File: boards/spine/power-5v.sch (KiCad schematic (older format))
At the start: 15 parts, among them U8 RT8299A

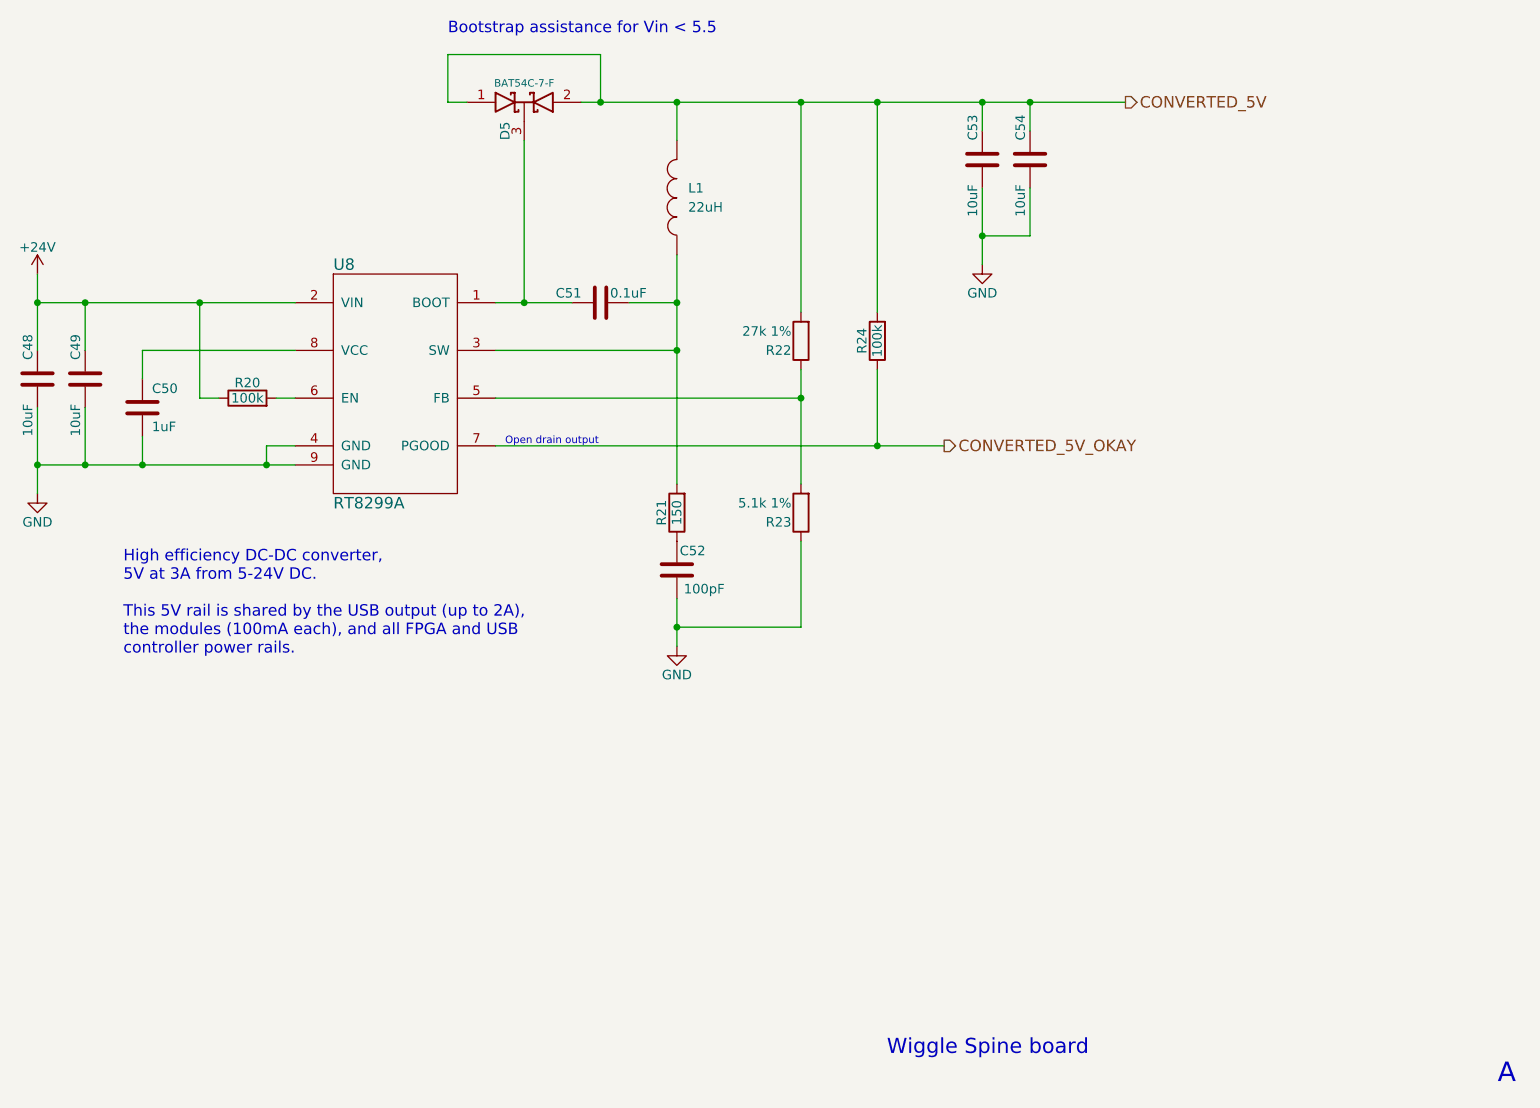
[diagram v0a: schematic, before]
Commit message: Capacitor upgrades, BOM tidying
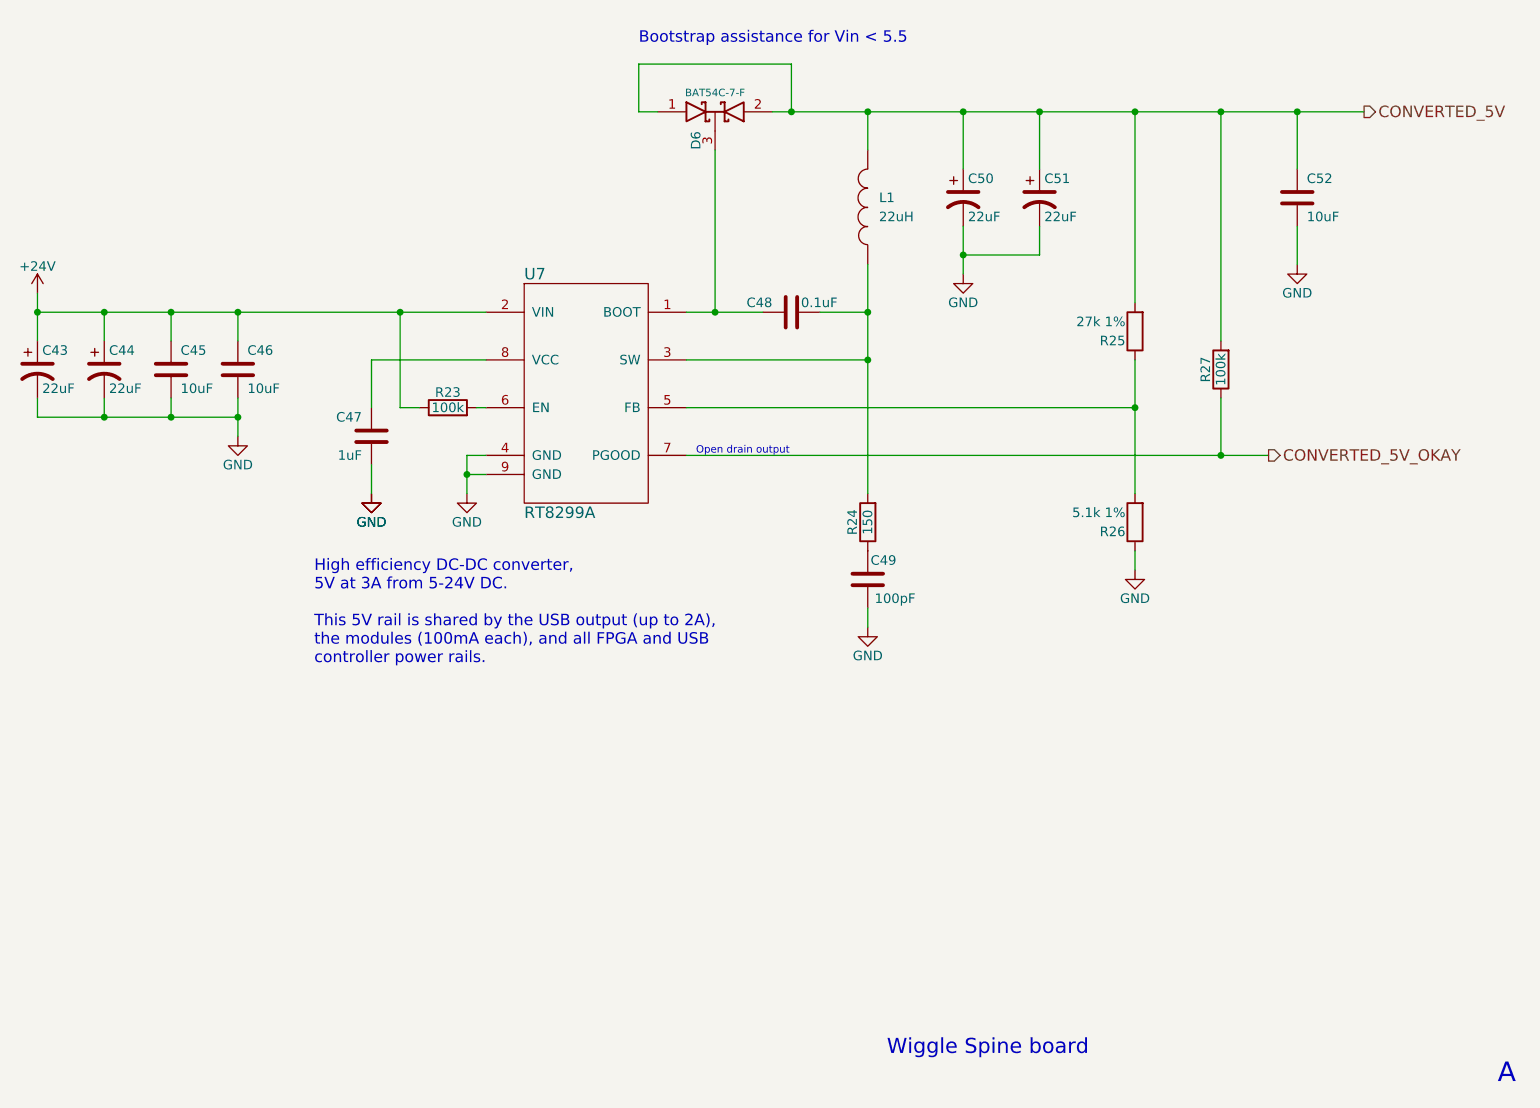
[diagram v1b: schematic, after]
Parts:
- removed C48, C49, C53, C54: 10uF, Capacitors_SMD:C_1206, symbol C
- added C43, C44, C50, C51: 22uF, Capacitors_SMD:c_elec_6.3x7.7, symbol CP1
- added C45, C46, C52: 10uF, Capacitors_SMD:C_1206, symbol C
- C47: renamed from C50; value 1uF -> 1uF
- renumbered C51 to C48, C52 to C49, D5 to D6, R20 to R23, R21 to R24, R22 to R25, R23 to R26, R24 to R27, U8 to U7
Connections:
- net +24V: now also C43.1, C44.1, C45.1, C46.1
- net CONVERTED_5V: now also C50.1, C51.1, C52.1
- net GND: now also C43.2, C44.2, C45.2, C46.2, C50.2, C51.2, C52.2
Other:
- moved on the sheet: C47, C48, C49, D6, L1, R23, R24, R25, R26, R27, U7

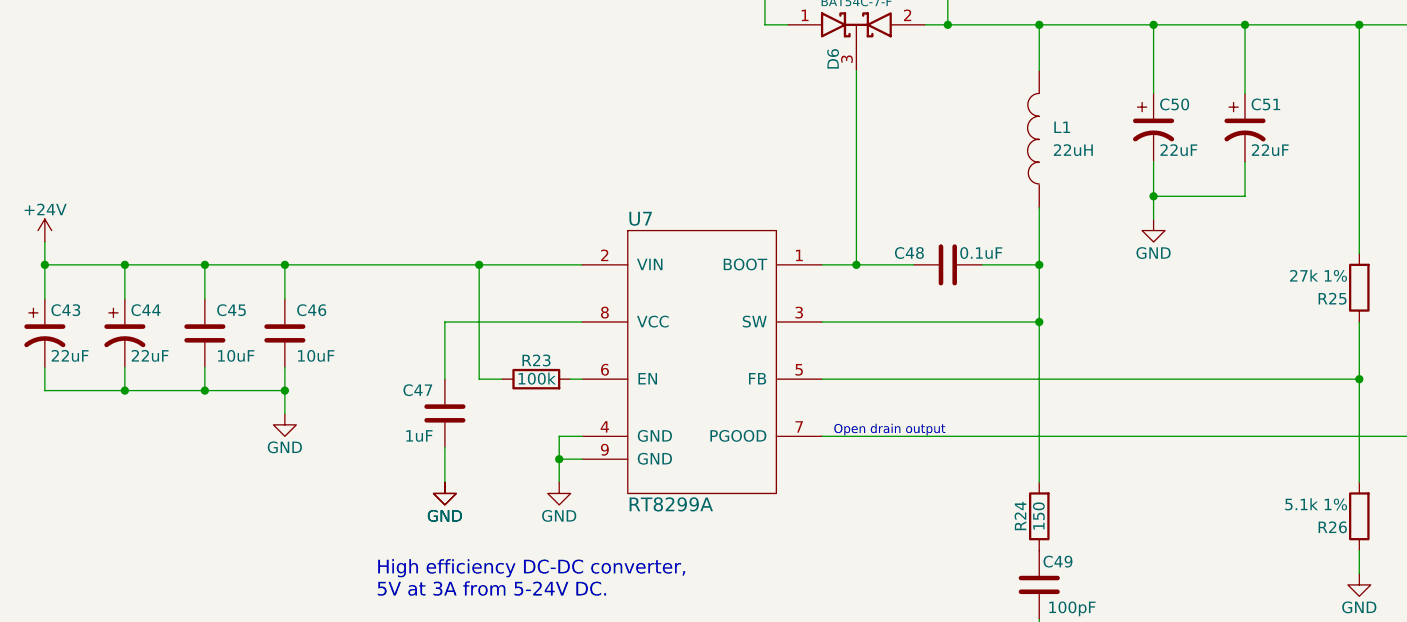
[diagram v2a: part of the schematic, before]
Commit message: Schematics stabilizing for next proto, starting PCB updates
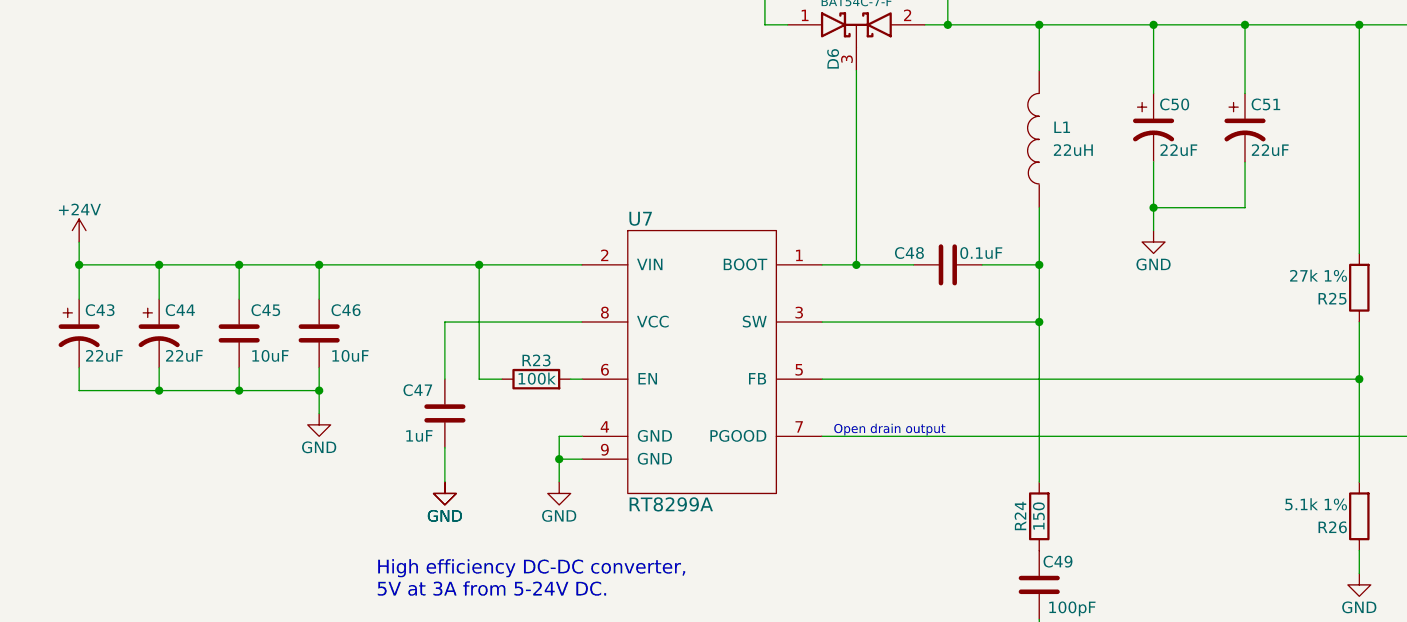
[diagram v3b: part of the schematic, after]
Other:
- moved on the sheet: C43, C44, C45, C46
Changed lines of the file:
@@
 L +24V #PWR0123
 U 1 1 564CA8DB
-P 2250 3750
-F 0 "#PWR0123" H 2250 3600 50  0001 C CNN
-F 1 "+24V" H 2250 3890 50  0000 C CNN
-F 2 "" H 2250 3750 60  0000 C CNN
-F 3 "" H 2250 3750 60  0000 C CNN
-	1    2250 3750
+P 2400 3750
+F 0 "#PWR0123" H 2400 3600 50  0001 C CNN
+F 1 "+24V" H 2400 3890 50  0000 C CNN
+F 2 "" H 2400 3750 60  0000 C CNN
+F 3 "" H 2400 3750 60  0000 C CNN
+	1    2400 3750
 	1    0    0    -1
 $EndComp
@@
 FB 59 00 E6 A5 69 3A 37 9E CF 73 BC F7 37 E3 33 5D 9E A8 3E 7F 80 FA F7 F6 BB 44 F4 6E D4 E7 77
 A2 1E 1F 27 A2 E3 16 70 32 E9 54 FE 3F E7 AF 00 CA 1C A3 36 0A 00 00 00 00 49 45 4E 44 AE 42 60
-82 00
+82 70
 EndData
 $EndBitmap
@@
 L GND #PWR0126
 U 1 1 567A1422
-P 7100 3650
-F 0 "#PWR0126" H 7100 3400 50  0001 C CNN
-F 1 "GND" H 7100 3500 50  0000 C CNN
-F 2 "" H 7100 3650 60  0000 C CNN
-F 3 "" H 7100 3650 60  0000 C CNN
-	1    7100 3650
+P 7100 3700
+F 0 "#PWR0126" H 7100 3450 50  0001 C CNN
+F 1 "GND" H 7100 3550 50  0000 C CNN
+F 2 "" H 7100 3700 60  0000 C CNN
+F 3 "" H 7100 3700 60  0000 C CNN
+	1    7100 3700
 	1    0    0    -1
 $EndComp
@@
 Wire Wire Line
 	4000 4100 4600 4100
-Connection ~ 3300 3850
-Wire Wire Line
-	3300 3850 3300 4000
-Wire Wire Line
-	2250 3850 4600 3850
+Connection ~ 3450 3850
+Wire Wire Line
+	3450 3850 3450 4000
 Wire Wire Line
 	5650 3850 6050 3850
 Wire Wire Line
-	4150 4350 4150 3850
+	4150 3850 4150 4350
 Connection ~ 4150 3850
 Wire Wire Line
-	7100 3400 7100 3650
-Wire Wire Line
-	7100 3550 7500 3550
-Wire Wire Line
-	7500 3550 7500 3400
-Connection ~ 7100 3550
+	7100 3400 7100 3700
+Wire Wire Line
+	7100 3600 7500 3600
+Wire Wire Line
+	7500 3600 7500 3400
+Connection ~ 7100 3600
 Wire Wire Line
 	7100 3100 7100 2800
@@
 	4550 4350 4600 4350
 Wire Wire Line
-	4250 4350 4150 4350
+	4150 4350 4250 4350
 $Comp
 L CP1 C43
 U 1 1 567A2C4C
-P 2250 4150
-F 0 "C43" H 2275 4250 50  0000 L CNN
-F 1 "22uF" H 2275 4050 50  0000 L CNN
-F 2 "Capacitors_SMD:c_elec_6.3x7.7" H 2250 4150 60  0001 C CNN
-F 3 "http://nichicon-us.com/english/products/pdfs/e-cd.pdf" H 2250 4150 60  0001 C CNN
-F 4 "Digikey" H 2250 4150 60  0001 C CNN "Vend1"
-F 5 "493-6180-2-ND" H 2250 4150 60  0001 C CNN "Vend1Id"
-F 6 "Nichicon" H 2250 4150 60  0001 C CNN "Mfg1"
-F 7 "UCD1H220MCL1GS" H 2250 4150 60  0001 C CNN "Mfg1Id"
-F 8 "0.10868" H 2250 4150 60  0001 C CNN "RefPrice1k"
-	1    2250 4150
+P 2400 4150
+F 0 "C43" H 2425 4250 50  0000 L CNN
+F 1 "22uF" H 2425 4050 50  0000 L CNN
+F 2 "Capacitors_SMD:c_elec_6.3x7.7" H 2400 4150 60  0001 C CNN
+F 3 "http://nichicon-us.com/english/products/pdfs/e-cd.pdf" H 2400 4150 60  0001 C CNN
+F 4 "Digikey" H 2400 4150 60  0001 C CNN "Vend1"
+F 5 "493-6180-2-ND" H 2400 4150 60  0001 C CNN "Vend1Id"
+F 6 "Nichicon" H 2400 4150 60  0001 C CNN "Mfg1"
+F 7 "UCD1H220MCL1GS" H 2400 4150 60  0001 C CNN "Mfg1Id"
+F 8 "0.10868" H 2400 4150 60  0001 C CNN "RefPrice1k"
+	1    2400 4150
 	1    0    0    -1
 $EndComp
@@
 L CP1 C44
 U 1 1 567A2CD8
-P 2600 4150
-F 0 "C44" H 2625 4250 50  0000 L CNN
-F 1 "22uF" H 2625 4050 50  0000 L CNN
-F 2 "Capacitors_SMD:c_elec_6.3x7.7" H 2600 4150 60  0001 C CNN
-F 3 "http://nichicon-us.com/english/products/pdfs/e-cd.pdf" H 2600 4150 60  0001 C CNN
-F 4 "Digikey" H 2600 4150 60  0001 C CNN "Vend1"
-F 5 "493-6180-2-ND" H 2600 4150 60  0001 C CNN "Vend1Id"
-F 6 "Nichicon" H 2600 4150 60  0001 C CNN "Mfg1"
-F 7 "UCD1H220MCL1GS" H 2600 4150 60  0001 C CNN "Mfg1Id"
-F 8 "0.10868" H 2600 4150 60  0001 C CNN "RefPrice1k"
-	1    2600 4150
+P 2750 4150
+F 0 "C44" H 2775 4250 50  0000 L CNN
+F 1 "22uF" H 2775 4050 50  0000 L CNN
+F 2 "Capacitors_SMD:c_elec_6.3x7.7" H 2750 4150 60  0001 C CNN
+F 3 "http://nichicon-us.com/english/products/pdfs/e-cd.pdf" H 2750 4150 60  0001 C CNN
+F 4 "Digikey" H 2750 4150 60  0001 C CNN "Vend1"
+F 5 "493-6180-2-ND" H 2750 4150 60  0001 C CNN "Vend1Id"
+F 6 "Nichicon" H 2750 4150 60  0001 C CNN "Mfg1"
+F 7 "UCD1H220MCL1GS" H 2750 4150 60  0001 C CNN "Mfg1Id"
+F 8 "0.10868" H 2750 4150 60  0001 C CNN "RefPrice1k"
+	1    2750 4150
 	1    0    0    -1
 $EndComp
@@
 L C C46
 U 1 1 567A30F9
-P 3300 4150
-F 0 "C46" H 3350 4250 50  0000 L CNN
-F 1 "10uF " H 3350 4050 50  0000 L CNN
-F 2 "Capacitors_SMD:C_1206" H 3338 4000 30  0001 C CNN
-F 3 "http://www.murata.com/~/media/webrenewal/support/library/catalog/products/capacitor/mlcc/c02e.ashx" H 3300 4150 60  0001 C CNN
-F 4 "GRM31CR61H106MA12L" H 3350 3950 39  0001 L BNN "Mfg1Id"
-F 5 "Murata" H 3300 4150 60  0001 C CNN "Mfg1"
-F 6 "Digikey" H 3300 4150 60  0001 C CNN "Vend1"
-F 7 "490-10756-2-ND" H 3300 4150 60  0001 C CNN "Vend1Id"
-F 8 "0.07429" H 3300 4150 60  0001 C CNN "RefPrice1k"
-	1    3300 4150
+P 3450 4150
+F 0 "C46" H 3500 4250 50  0000 L CNN
+F 1 "10uF " H 3500 4050 50  0000 L CNN
+F 2 "Capacitors_SMD:C_1206" H 3488 4000 30  0001 C CNN
+F 3 "http://www.murata.com/~/media/webrenewal/support/library/catalog/products/capacitor/mlcc/c02e.ashx" H 3450 4150 60  0001 C CNN
+F 4 "GRM31CR61H106MA12L" H 3500 3950 39  0001 L BNN "Mfg1Id"
+F 5 "Murata" H 3450 4150 60  0001 C CNN "Mfg1"
+F 6 "Digikey" H 3450 4150 60  0001 C CNN "Vend1"
+F 7 "490-10756-2-ND" H 3450 4150 60  0001 C CNN "Vend1Id"
+F 8 "0.07429" H 3450 4150 60  0001 C CNN "RefPrice1k"
+	1    3450 4150
 	1    0    0    -1
 $EndComp
@@
 L GND #PWR0131
 U 1 1 567A3822
-P 3300 4500
-F 0 "#PWR0131" H 3300 4250 50  0001 C CNN
-F 1 "GND" H 3300 4350 50  0000 C CNN
-F 2 "" H 3300 4500 60  0000 C CNN
-F 3 "" H 3300 4500 60  0000 C CNN
-	1    3300 4500
+P 3450 4500
+F 0 "#PWR0131" H 3450 4250 50  0001 C CNN
+F 1 "GND" H 3450 4350 50  0000 C CNN
+F 2 "" H 3450 4500 60  0000 C CNN
+F 3 "" H 3450 4500 60  0000 C CNN
+	1    3450 4500
 	1    0    0    -1
 $EndComp
 Wire Wire Line
-	3300 4300 3300 4500
+	3450 4300 3450 4500
 $Comp
 L C C45
 U 1 1 567A3945
-P 2950 4150
-F 0 "C45" H 3000 4250 50  0000 L CNN
-F 1 "10uF " H 3000 4050 50  0000 L CNN
-F 2 "Capacitors_SMD:C_1206" H 2988 4000 30  0001 C CNN
-F 3 "http://www.murata.com/~/media/webrenewal/support/library/catalog/products/capacitor/mlcc/c02e.ashx" H 2950 4150 60  0001 C CNN
-F 4 "GRM31CR61H106MA12L" H 3000 3950 39  0001 L BNN "Mfg1Id"
-F 5 "Murata" H 2950 4150 60  0001 C CNN "Mfg1"
-F 6 "Digikey" H 2950 4150 60  0001 C CNN "Vend1"
-F 7 "490-10756-2-ND" H 2950 4150 60  0001 C CNN "Vend1Id"
-F 8 "0.07429" H 2950 4150 60  0001 C CNN "RefPrice1k"
-	1    2950 4150
+P 3100 4150
+F 0 "C45" H 3150 4250 50  0000 L CNN
+F 1 "10uF " H 3150 4050 50  0000 L CNN
+F 2 "Capacitors_SMD:C_1206" H 3138 4000 30  0001 C CNN
+F 3 "http://www.murata.com/~/media/webrenewal/support/library/catalog/products/capacitor/mlcc/c02e.ashx" H 3100 4150 60  0001 C CNN
+F 4 "GRM31CR61H106MA12L" H 3150 3950 39  0001 L BNN "Mfg1Id"
+F 5 "Murata" H 3100 4150 60  0001 C CNN "Mfg1"
+F 6 "Digikey" H 3100 4150 60  0001 C CNN "Vend1"
+F 7 "490-10756-2-ND" H 3100 4150 60  0001 C CNN "Vend1Id"
+F 8 "0.07429" H 3100 4150 60  0001 C CNN "RefPrice1k"
+	1    3100 4150
 	1    0    0    -1
 $EndComp
 Wire Wire Line
-	2250 4400 3300 4400
-Wire Wire Line
-	2950 4400 2950 4300
-Connection ~ 3300 4400
-Wire Wire Line
-	2600 4400 2600 4300
-Connection ~ 2950 4400
-Wire Wire Line
-	2250 4400 2250 4300
-Connection ~ 2600 4400
-Wire Wire Line
-	2950 3850 2950 4000
-Wire Wire Line
-	2600 3850 2600 4000
-Connection ~ 2950 3850
-Wire Wire Line
-	2250 3750 2250 4000
-Connection ~ 2600 3850
-Connection ~ 2250 3850
+	2400 4400 3450 4400
+Wire Wire Line
+	3100 4400 3100 4300
+Connection ~ 3450 4400
+Wire Wire Line
+	2750 4400 2750 4300
+Connection ~ 3100 4400
+Wire Wire Line
+	2400 4400 2400 4300
+Connection ~ 2750 4400
+Wire Wire Line
+	3100 3850 3100 4000
+Wire Wire Line
+	2750 3850 2750 4000
+Connection ~ 3100 3850
+Wire Wire Line
+	2400 3750 2400 4000
+Connection ~ 2750 3850
+Connection ~ 2400 3850
+Wire Wire Line
+	2400 3850 4600 3850
 $EndSCHEMATC
